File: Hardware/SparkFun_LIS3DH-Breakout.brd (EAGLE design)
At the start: 15.2 x 15.2 mm, 15 parts, among them U2 LIS3DH

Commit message: Finished design for proto 1
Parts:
- removed JP1: LOGO-SFESK, SparkFun:SFE-LOGO-FLAME
- removed JP5: (no value), SparkFun:1X06
- removed U$2: CREATIVE_COMMONS, SparkFun:CREATIVE_COMMONS
- added FRAME2: FRAME-LETTER, SparkFun-Aesthetics:CREATIVE_COMMONS
- added J1: (no value), SparkFun-Connectors:1X06
- added J2: (no value), SparkFun-Connectors:1X05
- added LOGO1: SFE_LOGO_FLAME.1_INCH, SparkFun-Aesthetics:SFE_LOGO_FLAME_.1
- added R4: 10k, SparkFun-Resistors:0603
- added SJ2: (no value), TestAperatures:PAD-JUMPER-3-3OF3_NC_BY_TRACE_YES_SILK_FULL_BOX
- R1, R2: value 10k -> 4.7k; device SparkFun:0402-RES -> SparkFun-Resistors:0603
- R3: device SparkFun:0402-RES -> SparkFun-Resistors:0603
- moved U$1 16.7 mm to (20.8, 1.65)
- moved R1 13.2 mm to (15.7, 6.86), turned to 0 degrees
- moved JP2 10.6 mm to (22.2, 0.64)
- moved JP4 9.92 mm to (20.3, 6.35)
- moved R2 7.57 mm to (9.53, 9.27)
- moved JP3 6.35 mm to (2.54, 6.35)
- moved C1 5.40 mm to (15.0, 3.56)
- moved R3 4.33 mm to (15.7, 9.14), turned to 0 degrees
- moved U2 4.02 mm to (11.4, 6.35), turned to 180 degrees
- moved C3 3.98 mm to (15.0, 4.57)
- moved SJ1 3.89 mm to (11.4, 6.86)
- moved JP6 3.05 mm to (0.64, 11.4)
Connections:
- new net ADC1: J2.1, U2.16
- new net ADC2: J2.2, U2.15
- new net ADC3: J2.3, U2.13
- new net CS: J1.6, R4.1, U2.8
- new net N$1: R2.2, SJ2.1
- new net N$2: R1.2, SJ2.3
- net 3.3V: now also J1.2, R4.2, SJ2.2; no longer JP5.1, R1.2, R2.2
- net GND: now also J1.1; no longer JP5.6
- net INT1: now also J2.5; no longer JP5.5
- net INT2: now also J2.4; no longer JP5.4
- net SA0: now also J1.5
- net SCL: now also J1.4; no longer JP5.3
- net SDA: now also J1.3; no longer JP5.2
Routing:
- net N$1: track 0.00 -> 9.81 mm, vias 0 -> 1
- net N$2: track 0.00 -> 9.78 mm, vias 0 -> 1
- net GND: track 13.0 -> 4.03 mm, vias 2 -> 7
- net CS: track 0.00 -> 7.61 mm
- net ADC1: track 0.00 -> 6.47 mm, vias 0 -> 1
- net SCL: track 14.2 -> 7.81 mm, vias 2 -> 1
- net ADC3: track 0.00 -> 5.41 mm
- net ADC2: track 0.00 -> 5.03 mm, vias 0 -> 1
- net INT1: track 6.53 -> 9.23 mm, vias 0 -> 1
- net INT2: track 5.89 -> 8.46 mm
- net SDA: track 9.07 -> 10.2 mm, vias 0 -> 1
- net 3.3V: track 25.5 -> 24.8 mm, vias 1 -> 3
- net SA0: track 11.6 -> 11.0 mm, vias 2 -> 1
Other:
- board size 15.2 x 15.2 mm -> 22.9 x 12.7 mm
- board text added: "A1"
- board text added: "A2"
- board text added: "A3"
- board text added: "ADR"
- board text added: "CS"
- board text added: "Marshall Taylor"
- board text added: "PU EN"
- board text added: "SCL SCK"
- board text added: "SDA SDI"
- board text added: "SDO"
- board text added: "v01"
- board text removed: "10/17/11"
- board text removed: "SA0"

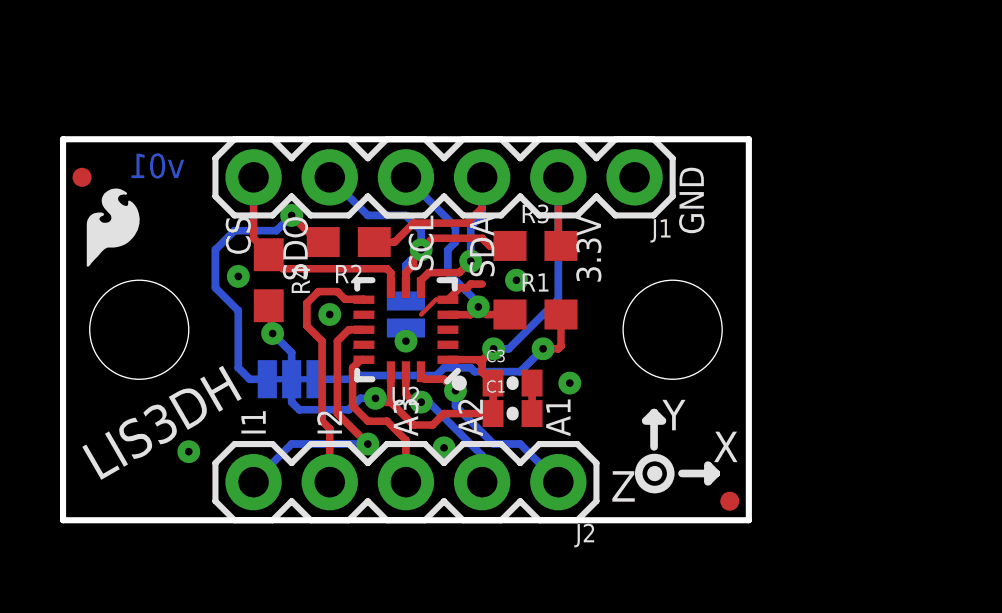
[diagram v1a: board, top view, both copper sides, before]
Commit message: Updated design based off design review
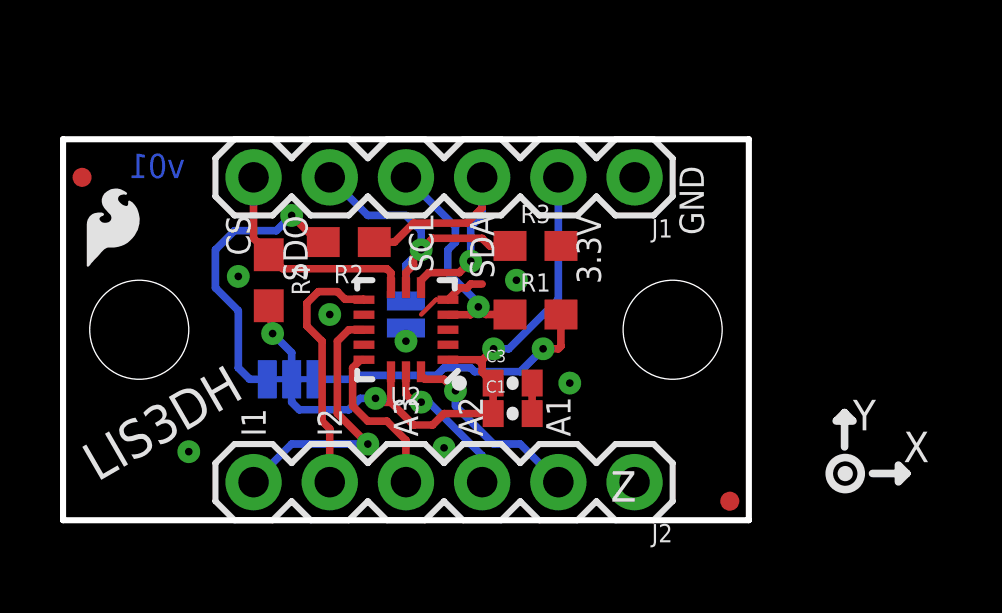
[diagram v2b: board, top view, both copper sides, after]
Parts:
- J2: device SparkFun-Connectors:1X05 -> SparkFun-Connectors:1X06
- moved U$1 19.9 mm to (2.54, 9.53)
- moved J2 2.54 mm to (19.1, 1.27)
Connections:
- new net VCC: J1.2
- net 3.3V: no longer J1.2
- net ADC1: now also J2.2; no longer J2.1
- net ADC2: now also J2.3; no longer J2.2
- net ADC3: now also J2.4; no longer J2.3
- net GND: now also J2.1
- net INT1: now also J2.6; no longer J2.5
- net INT2: now also J2.5; no longer J2.4
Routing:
- net 3.3V: track 24.8 -> 22.6 mm

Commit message: Adjusted a trace and updated components to most recent libraries
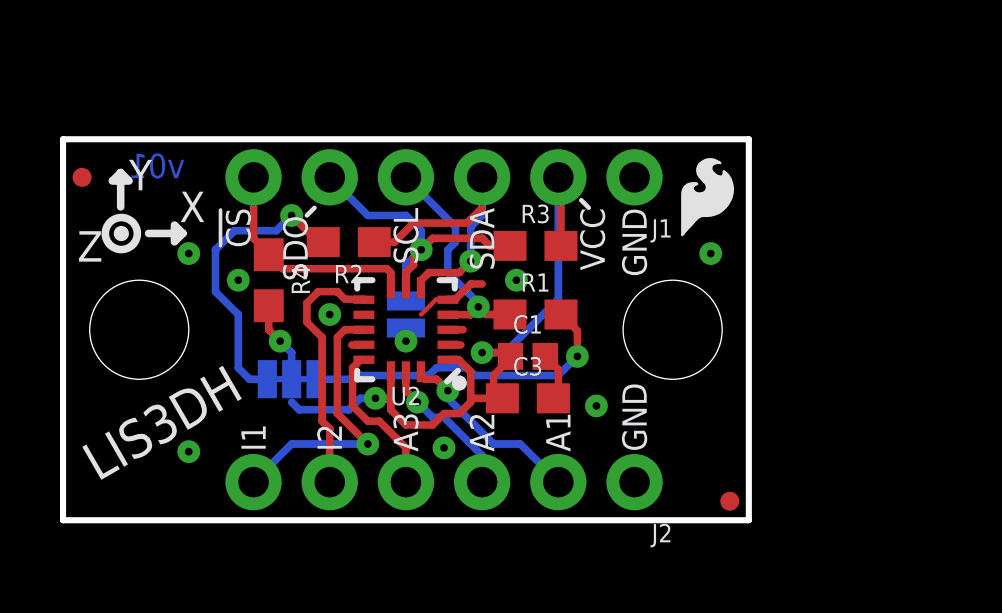
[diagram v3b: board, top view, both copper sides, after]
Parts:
- C1: device SparkFun:0402-CAP -> SparkFun-Capacitors:0402
- C3: value 4.7uF -> 10uF; device SparkFun:0402-CAP -> SparkFun-Capacitors:0603
- J1, J2: device SparkFun-Connectors:1X06 -> SparkFun-Connectors:1X06_NO_SILK
- moved LOGO1 19.8 mm to (20.3, 9.14)
- moved C1 1.97 mm to (15.5, 5.46)
- moved C3 0.72 mm to (15.5, 4.06)
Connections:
- net CS renamed !CS
- removed net 3.3V: C1.1, C3.1, R3.2, R4.2, SJ2.2, U2.1, U2.14
- net VCC: now also C1.1, C3.1, R3.2, R4.2, SJ2.2, U2.1, U2.14
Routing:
- net VCC: track 0.00 -> 26.4 mm, vias 0 -> 3
- net 3.3V: track 22.6 -> 0.00 mm, vias 3 -> 0
- net N$2: track 9.78 -> 10.9 mm
- net GND: track 4.03 -> 4.66 mm, vias 7 -> 9
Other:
- board text added: "!CS"
- board text added: "VCC"
- board text removed: "3.3V"
- board text removed: "CS"

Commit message: fixed airwire and renamed C3 to C2
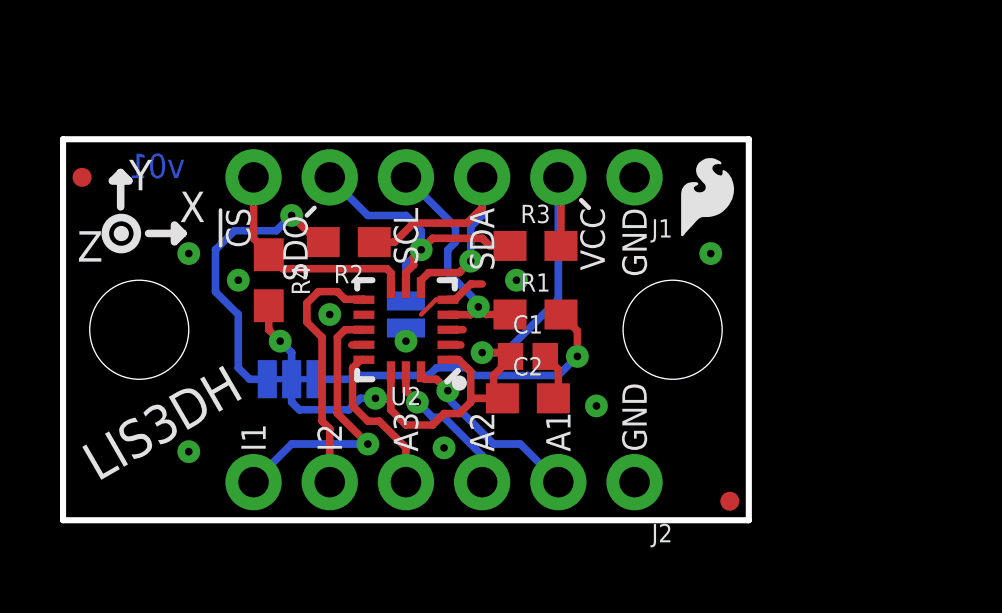
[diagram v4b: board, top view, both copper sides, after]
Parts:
- renumbered C3 to C2
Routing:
- net VCC: track 26.4 -> 27.1 mm

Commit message: Fixed silk: added address/jumper function, pumped up the product name silk.  Swapped I1 and I2.  Added more topside labeling
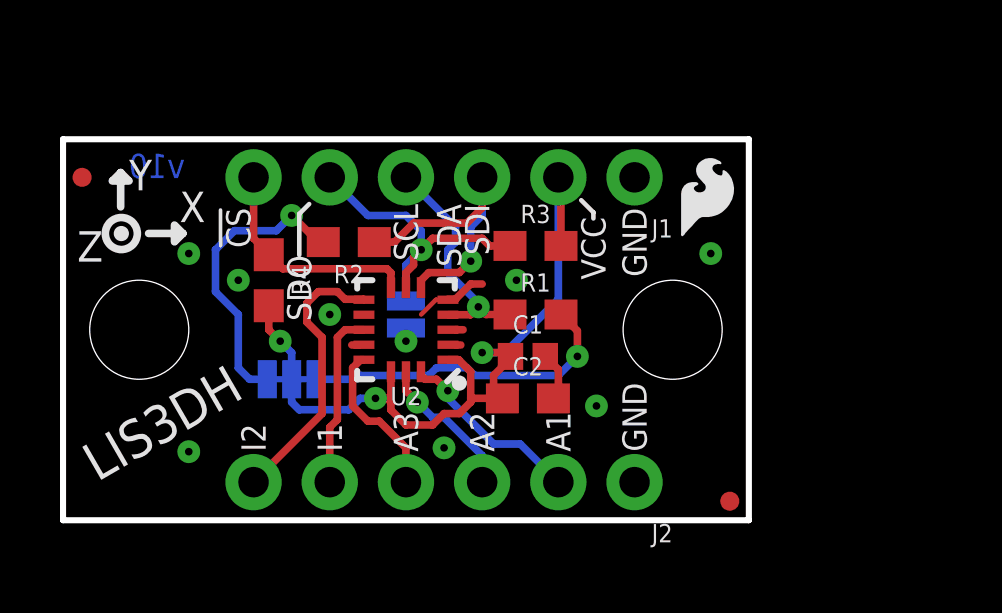
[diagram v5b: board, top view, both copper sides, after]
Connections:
- net INT1: now also J2.5; no longer J2.6
- net INT2: now also J2.6; no longer J2.5
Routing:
- net INT1: track 9.30 -> 5.92 mm, vias 1 -> 0
- net INT2: track 8.46 -> 9.30 mm
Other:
- board text added: "CLOSED: 0x18"
- board text added: "OPEN: 0x19/SPI"
- board text added: "v10"
- board text removed: "SDA"
- board text removed: "v01"

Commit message: removed 'ADR' and : silks
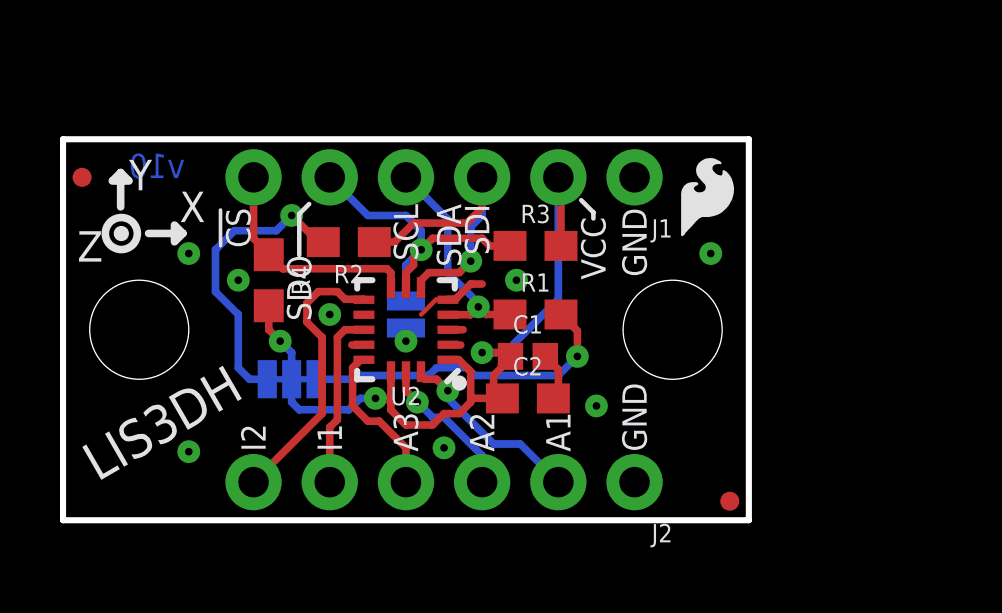
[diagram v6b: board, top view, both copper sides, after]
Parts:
- added LOGO2: SFE_LOGO_FLAME.1_INCH, SparkFun-Aesthetics:SFE_LOGO_FLAME_.1
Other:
- board text added: "CLOSED 0x18"
- board text added: "OPEN 0x19/SPI"
- board text removed: "ADR"
- board text removed: "CLOSED: 0x18"
- board text removed: "OPEN: 0x19/SPI"
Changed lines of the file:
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@@
 <grid distance="0.05" unitdist="inch" unit="inch" style="lines" multiple="1" display="yes" altdistance="0.001" altunitdist="inch" altunit="inch"/>
 <layers>
-<layer number="1" name="Top" color="4" fill="1" visible="yes" active="yes"/>
+<layer number="1" name="Top" color="4" fill="1" visible="no" active="yes"/>
 <layer number="2" name="Route2" color="1" fill="3" visible="no" active="no"/>
 <layer number="3" name="Route3" color="4" fill="3" visible="no" active="no"/>
@@
 <layer number="20" name="Dimension" color="15" fill="1" visible="yes" active="yes"/>
 <layer number="21" name="tPlace" color="16" fill="1" visible="no" active="yes"/>
-<layer number="22" name="bPlace" color="15" fill="1" visible="no" active="yes"/>
+<layer number="22" name="bPlace" color="14" fill="1" visible="yes" active="yes"/>
 <layer number="23" name="tOrigins" color="15" fill="1" visible="no" active="yes"/>
 <layer number="24" name="bOrigins" color="15" fill="1" visible="no" active="yes"/>
@@
 <text x="19.05" y="10.414" size="0.8128" layer="21" font="vector" ratio="15" rot="R270" align="center-left">GND</text>
 <text x="1.143" y="1.27" size="1.27" layer="21" font="vector" ratio="18" rot="SR30">LIS3DH</text>
-<text x="12.446" y="4.826" size="0.8128" layer="22" font="vector" ratio="15" rot="MR0">ADR</text>
 <text x="13.97" y="2.286" size="0.8128" layer="21" font="vector" ratio="15" rot="R90" align="center-left">A2</text>
 <text x="6.35" y="2.286" size="0.8128" layer="21" font="vector" ratio="15" rot="R90" align="center-left">I2</text>
@@
 <wire x1="7.874" y1="10.2108" x2="8.2042" y2="10.541" width="0.1524" layer="21"/>
 <wire x1="17.6784" y1="10.2616" x2="17.272" y2="10.668" width="0.1524" layer="21"/>
-<text x="10.16" y="6.858" size="0.8128" layer="22" font="vector" ratio="15" distance="10" rot="MR0" align="center-left">OPEN:
+<text x="10.16" y="6.858" size="0.8128" layer="22" font="vector" ratio="15" distance="10" rot="MR0" align="center-left">OPEN
 0x19/SPI</text>
-<text x="12.573" y="6.858" size="0.8128" layer="22" font="vector" ratio="15" distance="10" rot="MR0" align="center-right">CLOSED:
+<text x="12.5222" y="6.858" size="0.8128" layer="22" font="vector" ratio="15" distance="10" rot="MR0" align="center-right">CLOSED
 0x18</text>
 <wire x1="7.874" y1="8.8392" x2="7.874" y2="10.2108" width="0.1524" layer="21"/>
@@
 <attribute name="PROD_ID" value="CONN-08437" x="19.05" y="1.27" size="1.778" layer="27" font="vector" ratio="15" rot="R180" display="off"/>
 </element>
+<element name="LOGO2" library="SparkFun-Aesthetics" package="SFE_LOGO_FLAME_.1" value="SFE_LOGO_FLAME.1_INCH" x="22.606" y="0.254" rot="MR0"/>
 </elements>
 <signals>
@@
 <wire x1="12.83" y1="6.85" x2="13.581" y2="6.85" width="0.254" layer="1"/>
 <wire x1="13.581" y1="6.85" x2="13.843" y2="7.112" width="0.254" layer="1"/>
-<wire x1="12.827" y1="8.255" x2="12.827" y2="9.017" width="0.254" layer="16"/>
-<wire x1="12.827" y1="9.017" x2="13.081" y2="9.271" width="0.254" layer="16"/>
-<wire x1="13.081" y1="9.271" x2="13.081" y2="9.779" width="0.254" layer="16"/>
-<wire x1="13.081" y1="9.779" x2="11.43" y2="11.43" width="0.254" layer="16"/>
+<wire x1="12.827" y1="8.255" x2="12.827" y2="10.033" width="0.254" layer="16"/>
+<wire x1="12.827" y1="10.033" x2="11.43" y2="11.43" width="0.254" layer="16"/>
 <wire x1="13.843" y1="7.112" x2="14.097" y2="6.858" width="0.254" layer="1"/>
 <wire x1="14.097" y1="6.858" x2="14.898" y2="6.858" width="0.254" layer="1"/>

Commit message: Applied review changes
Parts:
- moved JP2 0.36 mm to (22.0, 0.89)
- moved JP6 0.25 mm to (0.89, 11.4)
- renumbered U2 to U1
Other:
- board text added: "OPEN 0x19"
- board text removed: "OPEN 0x19/SPI"
